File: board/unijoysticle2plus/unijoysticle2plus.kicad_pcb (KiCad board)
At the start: 4 copper layers, 62 x 49 mm, 41 parts, among them J1 DB9_Female, J2 DB9_Female, J3 USB_B_Micro, Q1 MUN5211DW1, SW1 RESET, SW2 JOY SWAP, SW3 BOOT, U1 74HC05, U2 74HC05, U3 74HC05, U4 ESP32-WROOM-32E, U5 AMS1117-3.3, U6 CH340C

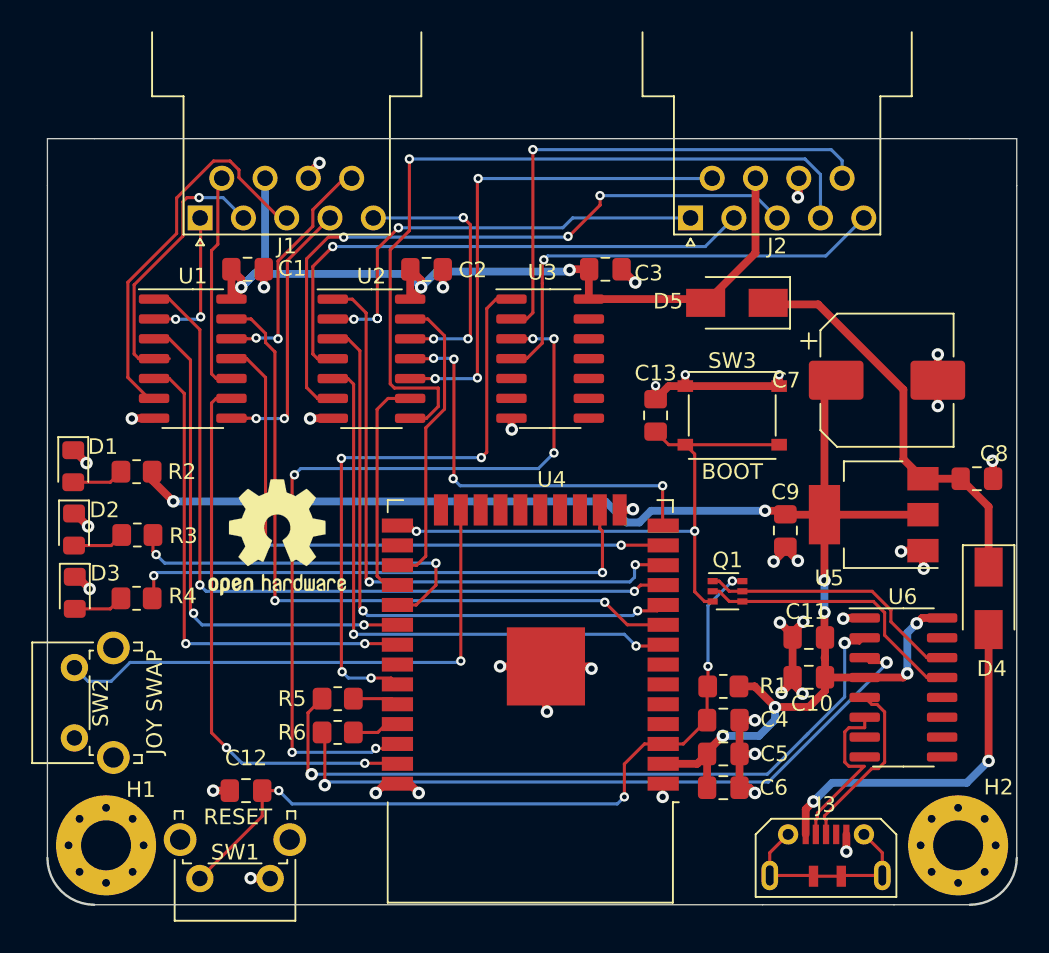
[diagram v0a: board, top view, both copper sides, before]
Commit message: Unijoysticle2+: Rev D
- Swap GPIO 12 & 13: issue #19
- Ground GPIO 4. This is to detect Uni2+
- Back to USB Micro B connector used in Rev. B
  - This is to avoid hand-soldering it.
  - Re-added the "hole" in PCB so that it can be placed using P&P
    machine.
- Reduced Green LED resistor from 1k to 330, this is to make it
  brighter.
- Auto reset circuit wasn't working on Rev C.
  Replaced it with original design, using S8050s.
  Fixed the pins, was broken in Rev A and Rev B.
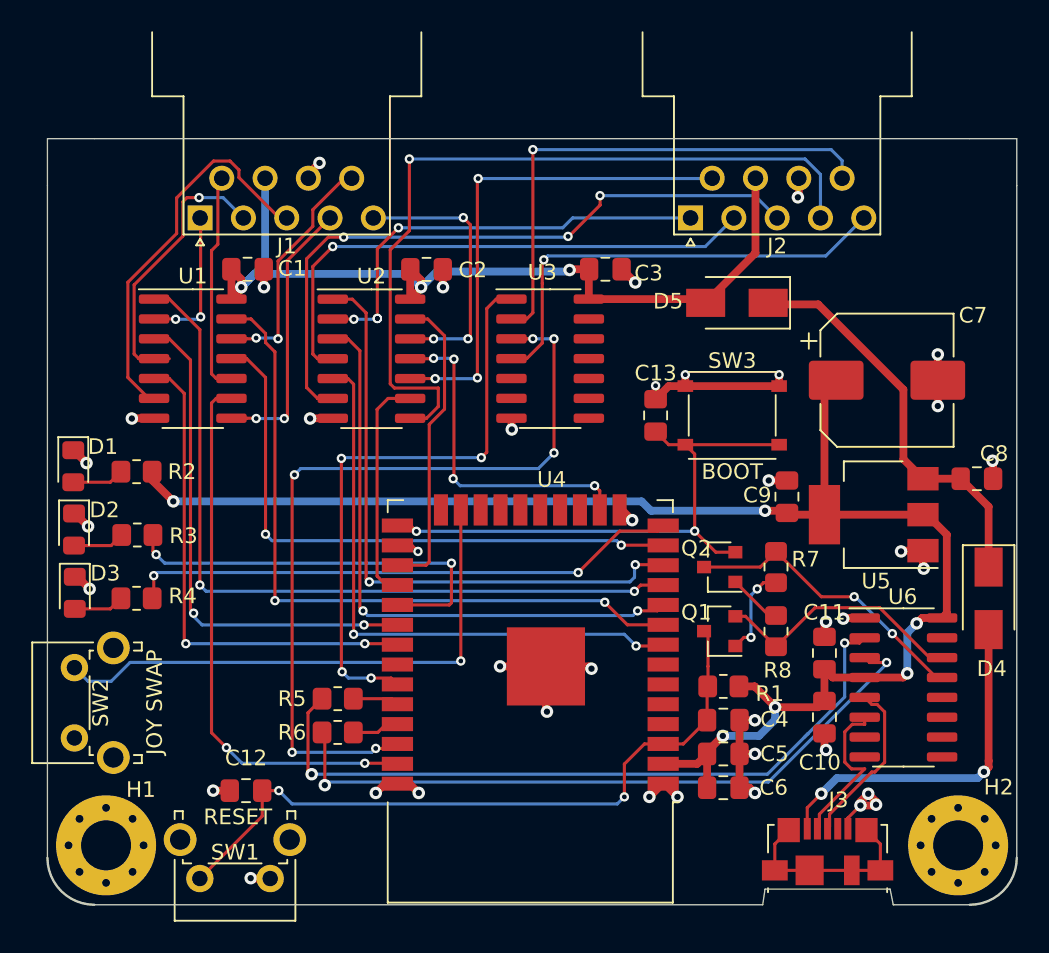
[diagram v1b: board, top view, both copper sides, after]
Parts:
- removed the REF** at (97.4, 124.8)
- added Q2: S8050, Package_TO_SOT_SMD:SOT-23, F.Cu at (125.7, 126.7)
- added R7: 10k, Resistor_SMD:R_0805_2012Metric_Pad1.20x1.40mm_HandSolder, F.Cu at (129.3, 126.7)
- added R8: 10k, Resistor_SMD:R_0805_2012Metric_Pad1.20x1.40mm_HandSolder, F.Cu at (129.3, 130.8)
- added REF**: OSHW-Logo2_14.6x12mm_SilkScreen, Symbol:OSHW-Logo2_14.6x12mm_SilkScreen, B.Cu at (89.8, 110.6)
- J3: footprint Unijoysticle:MicroXNJ -> Connector_USB:USB_Micro-B_Molex_47346-0001
- Q1: value MUN5211DW1 -> S8050; footprint Package_TO_SOT_SMD:SOT-363_SC-70-6 -> Package_TO_SOT_SMD:SOT-23
- R3: value 1k -> 330
- moved C10 2.74 mm to (132.4, 136.3), turned to 270 degrees
- moved Q1 2.60 mm to (125.7, 130.8), turned to 180 degrees
- moved C9 2.16 mm to (130.0, 122.2), turned to 90 degrees
- moved C11 1.41 mm to (132.4, 132.2), turned to 90 degrees
- moved J3 1.10 mm to (132.6, 144.9), turned to 0 degrees
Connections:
- Q1 pad 1: /RTS_PROG -> Net-(Q1-Pad1)
- Q1 pad 2: /DTR_PROG -> /RTS_PROG
- Q1 pad 3: /ESP_BOOT -> /ESP_EN
- U4 pad 14: /GPIO_J2_FIRE -> /GPIO_J2_LED
- U4 pad 16: /GPIO_J2_LED -> /GPIO_J2_FIRE
- U4 pad 26: (no net) -> GND
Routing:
- net Net-(Q1-Pad1): track 0.00 -> 5.86 mm, vias 0 -> 2
- net /GPIO_J2_FIRE: track 26.6 -> 21.4 mm
- net /ESP_EN: track 49.7 -> 45.4 mm, vias 4 -> 2
- net Net-(Q2-Pad1): track 0.00 -> 3.49 mm
- net +3V3: track 101.2 -> 98.6 mm, vias 8 -> 6
- net /GPIO_J1_LED: track 23.9 -> 26.5 mm
- net /ESP_BOOT: track 38.5 -> 36.4 mm
- net /DTR_PROG: track 17.8 -> 19.0 mm, vias 0 -> 2
- net /GPIO_J2_LED: track 34.3 -> 35.5 mm
- net Net-(J3-Pad6): track 13.5 -> 12.6 mm
- net /RTS_PROG: track 17.1 -> 16.4 mm
- net /USBD+: track 11.4 -> 10.8 mm
- net /USBD-: track 11.0 -> 10.4 mm
- net GND: track 68.3 -> 68.2 mm, vias 39 -> 40
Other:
- outline, holes or cut-outs redrawn
- board text added: "Unijoysticle 2+ Rev. D"
- board text removed: "Unijoysticle 2+ Rev. C"

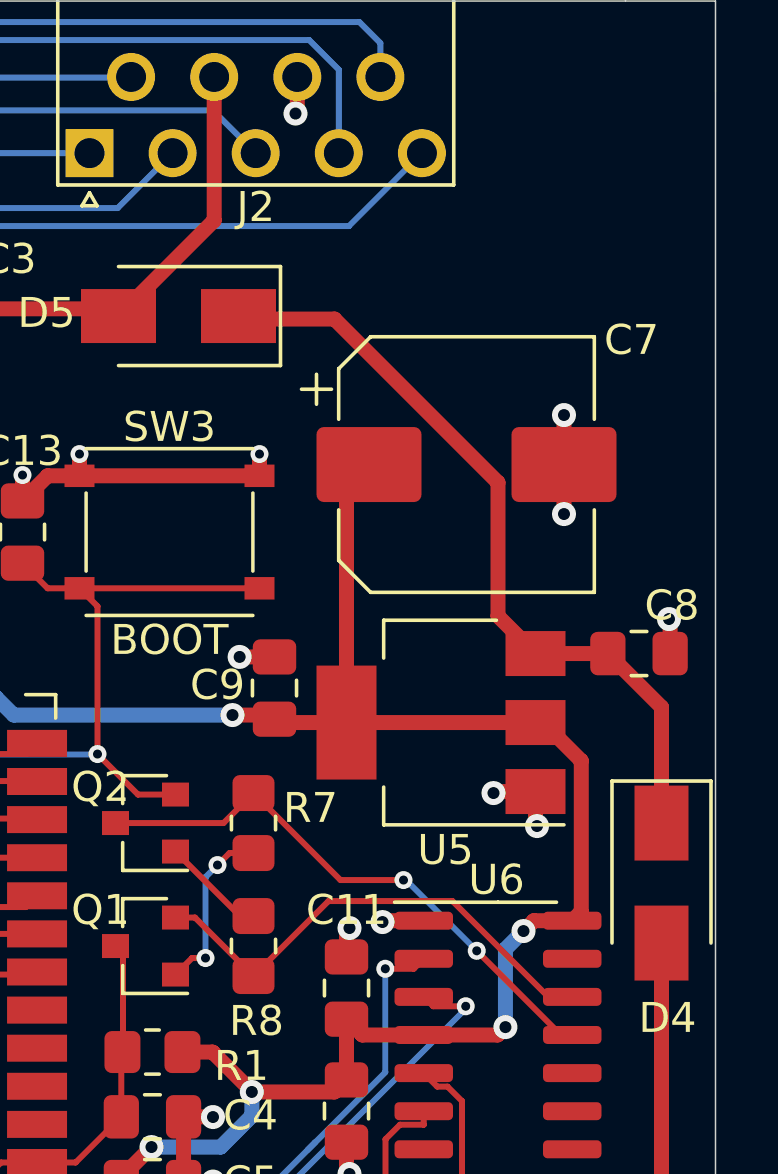
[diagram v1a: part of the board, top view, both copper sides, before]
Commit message: unijoysticle2+: place 1000uF cap differently
- Change footprint of 1000uF: bigger
- Place it slightly differently
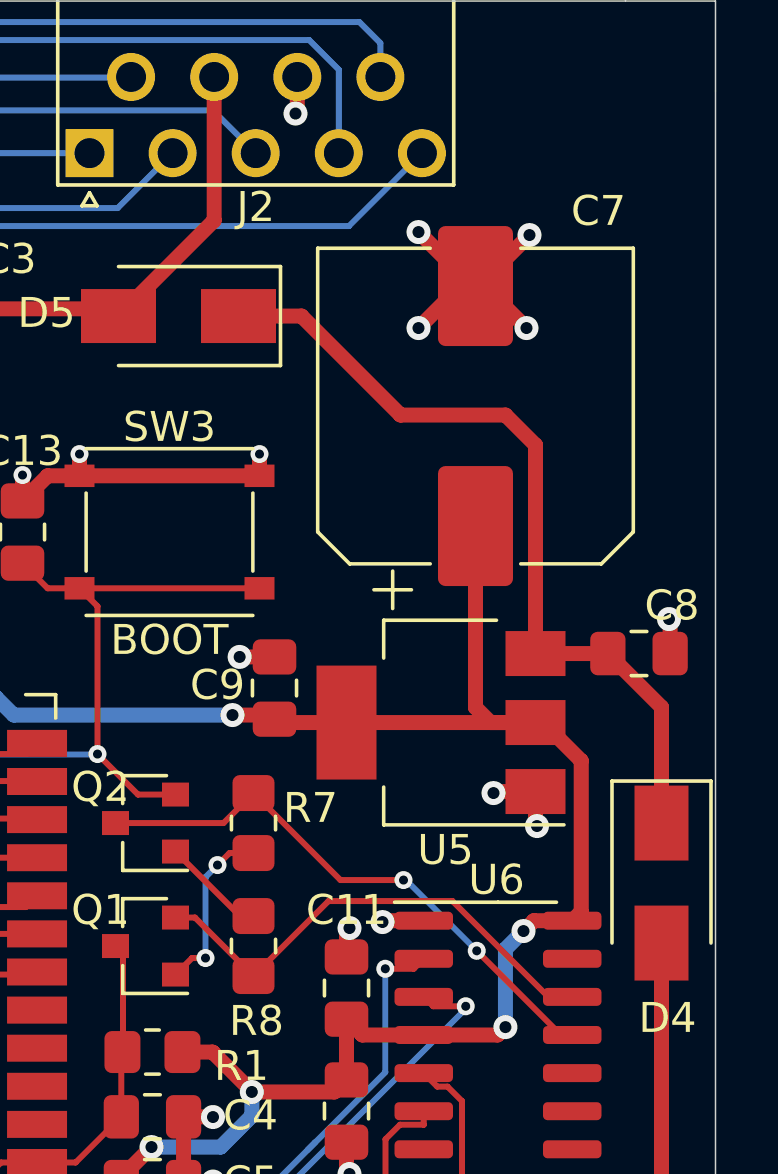
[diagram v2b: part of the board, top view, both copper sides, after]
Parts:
- C7: footprint Capacitor_SMD:CP_Elec_8x10 -> Capacitor_SMD:CP_Elec_10x10
- moved C7 1.97 mm to (136.7, 112.8), turned to 90 degrees
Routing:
- net GND: track 68.2 -> 74.8 mm, vias 40 -> 42
- net Net-(C8-Pad1): track 26.0 -> 27.4 mm
- net +3V3: track 98.6 -> 97.9 mm

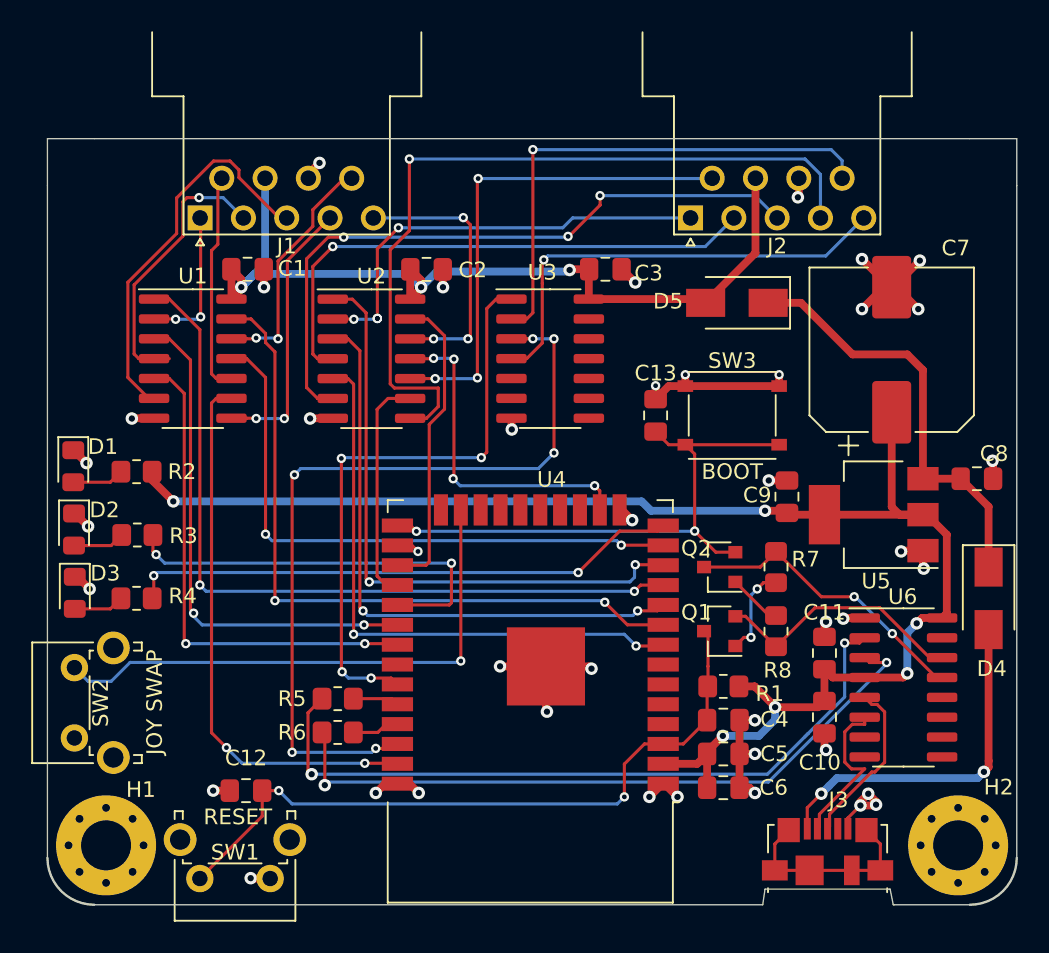
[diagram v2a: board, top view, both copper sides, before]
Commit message: Unijoysticle2+: Rev E
- Auto-reset circuit fixed: Transitor lines connected correctly
- Filter cap is between 5v and GND (and not +3.v3 and GND)
- Using 1.5K Ohm resistors for blue and red LEDs instead of 1K
- USB connector is just a tiny bit moved inwards
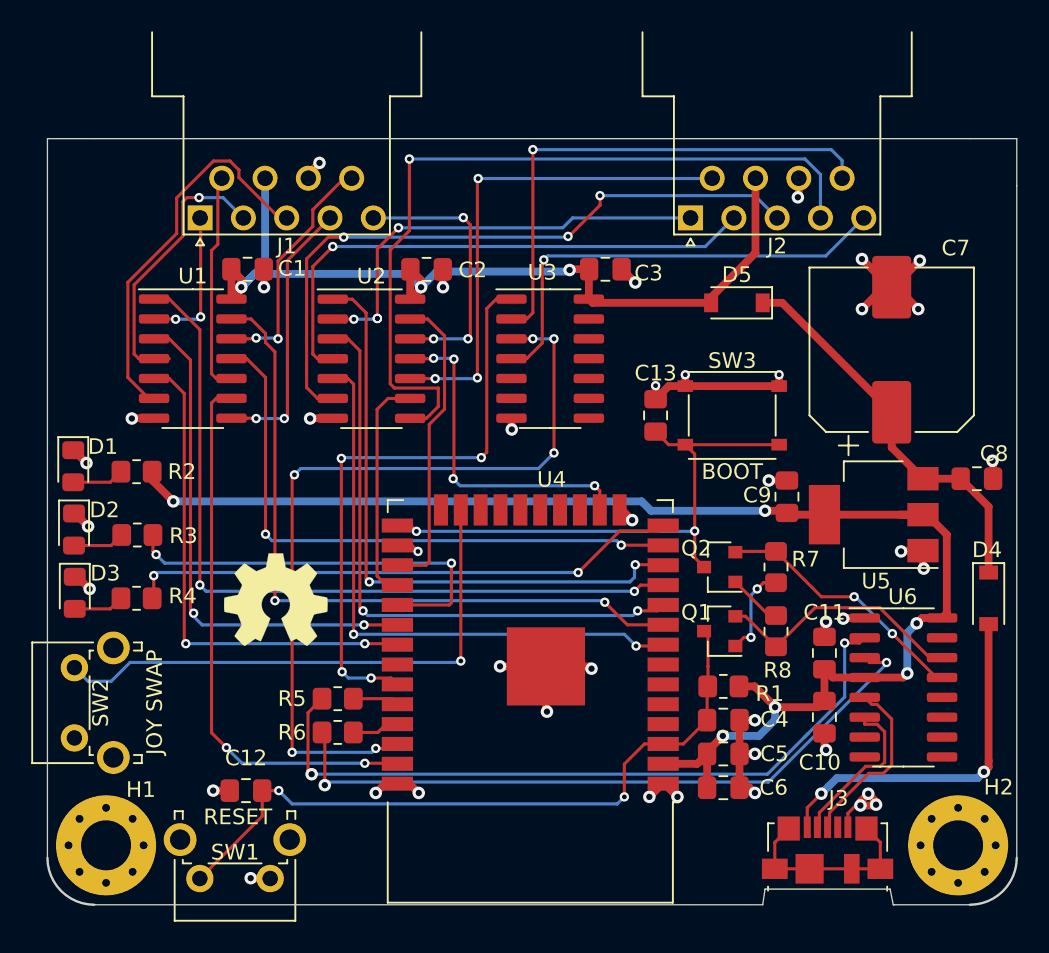
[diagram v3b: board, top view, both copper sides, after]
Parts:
- removed the REF** at (89.8, 110.6)
- added REF**: OSHW-Symbol_6.7x6mm_SilkScreen, Symbol:OSHW-Symbol_6.7x6mm_SilkScreen, F.Cu at (97.3, 128.8)
- D4, D5: footprint Diode_SMD:D_SMA -> Diode_SMD:D_SOD-123
- R2, R4: value 1k -> 1.5k
- moved J3 0.10 mm to (132.6, 144.8)
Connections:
- C7 pad 1: +3V3 -> Net-(C7-Pad1)
- C8 pad 1: Net-(C8-Pad1) -> Net-(C7-Pad1)
- D4 pad 1: Net-(C8-Pad1) -> Net-(C7-Pad1)
- D5 pad 1: Net-(C8-Pad1) -> Net-(C7-Pad1)
- Q2 pad 2: /ESP_BOOT -> /DTR_PROG
- Q2 pad 3: /DTR_PROG -> /ESP_BOOT
- U5 pad 3: Net-(C8-Pad1) -> Net-(C7-Pad1)
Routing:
- net Net-(C8-Pad1): track 27.4 -> 0.00 mm
- net Net-(C7-Pad1): track 0.00 -> 25.4 mm
- net +3V3: track 97.9 -> 91.1 mm
- net /DTR_PROG: track 19.0 -> 16.6 mm
- net /USBD+: track 10.8 -> 11.5 mm
- net /ESP_BOOT: track 36.4 -> 35.7 mm
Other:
- board text added: "Unijoysticle 2+ Rev. E"
- board text removed: "Unijoysticle 2+ Rev. D"

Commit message: Unijoysticle2+: Using CH340B instead of CH340C
CH340C is out of stock in JLCPCB. Using CH340B which is pin-compatible.
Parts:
- U6: value CH340C -> CH340B/C

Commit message: Unijoysticle 2+: use 10uF cap for C4
Instead of using .1uF cap for C4, it is replaced with a 10uF.
This fixes the autoboot issues.
Yay!
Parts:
- C4: value .1uF -> 10uF
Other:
- board text added: "Unijoysticle 2+ Rev. F"
- board text removed: "Unijoysticle 2+ Rev. E"

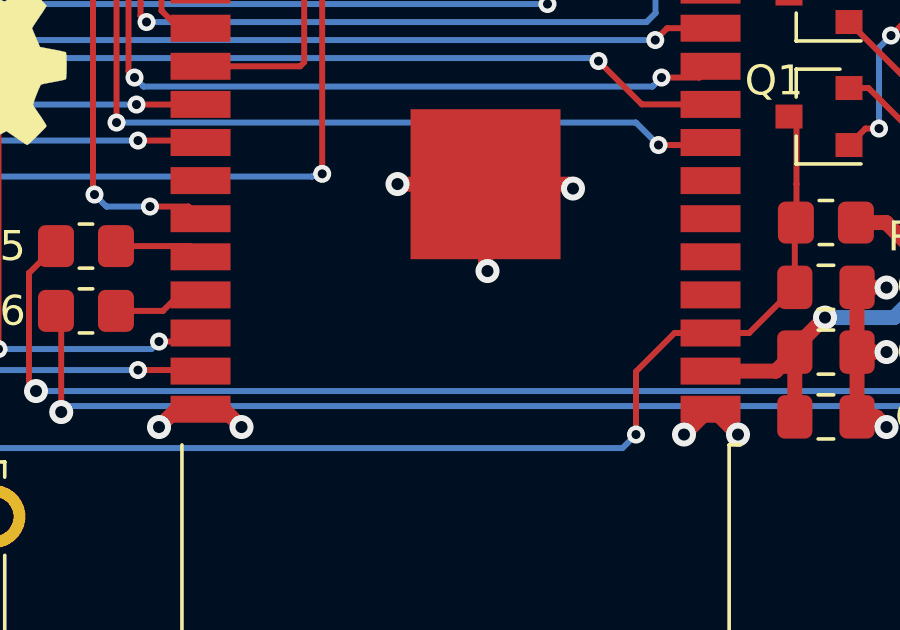
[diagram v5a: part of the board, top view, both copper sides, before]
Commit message: Unijoysticle2+: add text in schematic about ch340 and ESP32
Either CH340B or CH340C can be used.
And any ESP32-WROOM-32 can be used: 32, 32D or 32E (not the "U" variant
of course)
Add "JLCJLCJLCJLC" in silk screen to place the order number there.
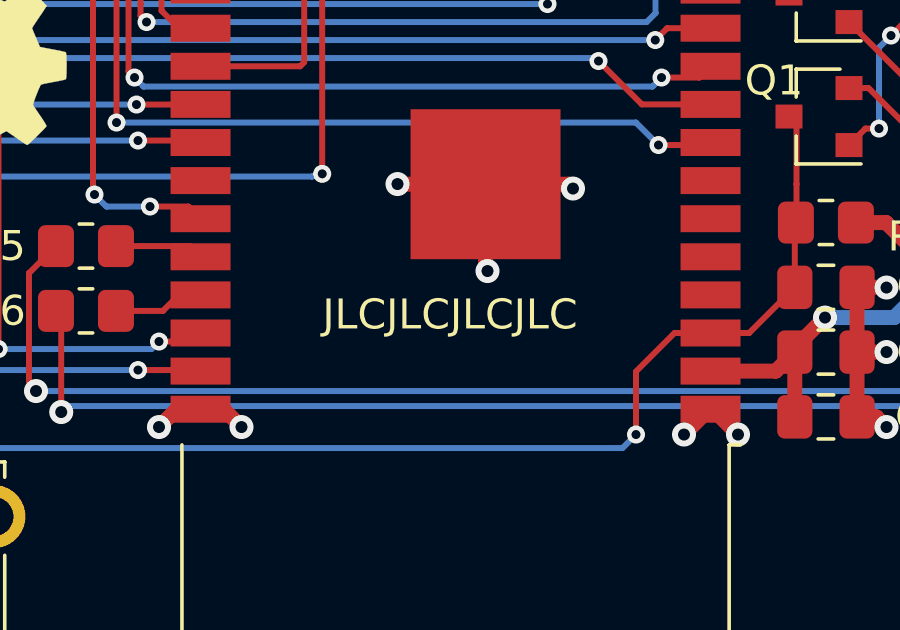
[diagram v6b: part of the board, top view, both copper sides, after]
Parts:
- U6: value CH340B/C -> CH340C
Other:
- board text added: "JLCJLCJLCJLC"
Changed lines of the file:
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@@
   (general
     (thickness 1.6)
-    (drawings 19)
+    (drawings 20)
     (tracks 685)
     (zones 0)
@@
       (drillshape 0)
       (scaleselection 1)
-      (outputdirectory "gerber_e/"))
+      (outputdirectory "gerber_f/"))
   )
   (net 0 "")
@@
     (add_net /ESP_RXD)
     (add_net /ESP_TXD)
-    (add_net /GPIO34)
-    (add_net /GPIO35)
-    (add_net /GPIO36)
-    (add_net /GPIO39)
     (add_net /GPIO_J1_DOWN)
     (add_net /GPIO_J1_FIRE)
@@
     (add_net "Net-(D2-Pad2)")
     (add_net "Net-(D3-Pad2)")
-    (add_net "Net-(J3-Pad4)")
     (add_net "Net-(J3-Pad6)")
     (add_net "Net-(Q1-Pad1)")
@@
     (add_net "Net-(R5-Pad2)")
     (add_net "Net-(R6-Pad2)")
-    (add_net "Net-(U4-Pad17)")
-    (add_net "Net-(U4-Pad18)")
-    (add_net "Net-(U4-Pad19)")
-    (add_net "Net-(U4-Pad20)")
-    (add_net "Net-(U4-Pad21)")
-    (add_net "Net-(U4-Pad22)")
-    (add_net "Net-(U4-Pad24)")
-    (add_net "Net-(U4-Pad32)")
-    (add_net "Net-(U6-Pad10)")
-    (add_net "Net-(U6-Pad11)")
-    (add_net "Net-(U6-Pad12)")
-    (add_net "Net-(U6-Pad15)")
-    (add_net "Net-(U6-Pad7)")
-    (add_net "Net-(U6-Pad8)")
-    (add_net "Net-(U6-Pad9)")
   )
   (net_class GND ""
@@
       (effects (font (size 1 1) (thickness 0.15)))
     )
-    (fp_text value CH340B/C (at 0 5.9) (layer F.Fab)
+    (fp_text value CH340C (at 0 5.9) (layer F.Fab)
       (effects (font (size 1 1) (thickness 0.15)))
     )
@@
     )
   )
+  (gr_text JLCJLCJLCJLC (at 113.435 137.43) (layer F.SilkS)
+    (effects (font (size 1 1) (thickness 0.15)))
+  )
   (gr_line (start 136.885 148.33) (end 136.835 148.33) (layer Edge.Cuts) (width 0.05))
